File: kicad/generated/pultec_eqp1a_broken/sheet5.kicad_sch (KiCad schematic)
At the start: 20 parts, among them T3 core

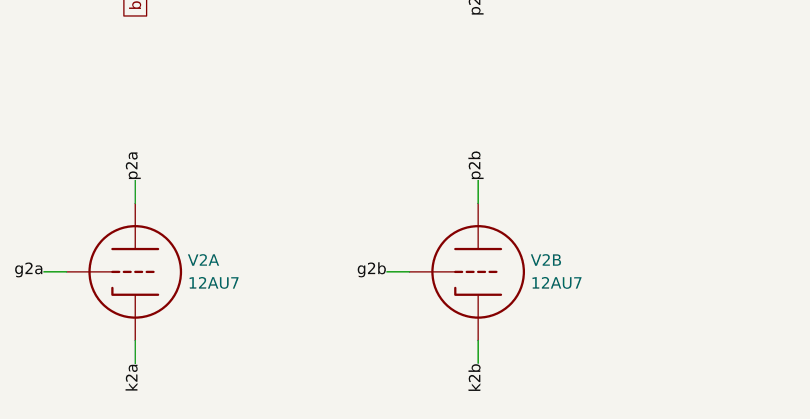
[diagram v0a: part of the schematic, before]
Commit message: Component editor C1: device files are pinned component versions
Device files move to config/components/<name>/<N>.yaml (the twelve former
config/devices/*.yaml are version 1, bytes unchanged), each version's sha256
(LF-normalized) in config/components/versions.lock. varimu/devices/versions.py
and varimu-circuit's versions.rs read the store the same way: a version edited
after saving is a load error, a bare name is the latest version for tools and
tests, and both builders refuse a bare name in a circuit. Circuits pin NAME@N:
the hand-written circuits, their device-choice parameters, the drawn circuits,
the symbol table's and both editors' placement defaults, the KiCad fixtures.
varimu fit-devices saves a new version only when a fit changed. The native
editor's model picker lists every version.

Every circuit builds identical IR and SPICE (export_circuit_fixtures --golden,
export_app_fixtures without a diff); the editor fixtures change only by the
pins. Tests: tests/test_versions.py, crates/varimu-circuit/tests/versions.rs,
editor_draw.rs (swapping a pinned version rebuilds; undo).

Co-Authored-By: Claude Opus 5.5 (1M context) <noreply@anthropic.com>
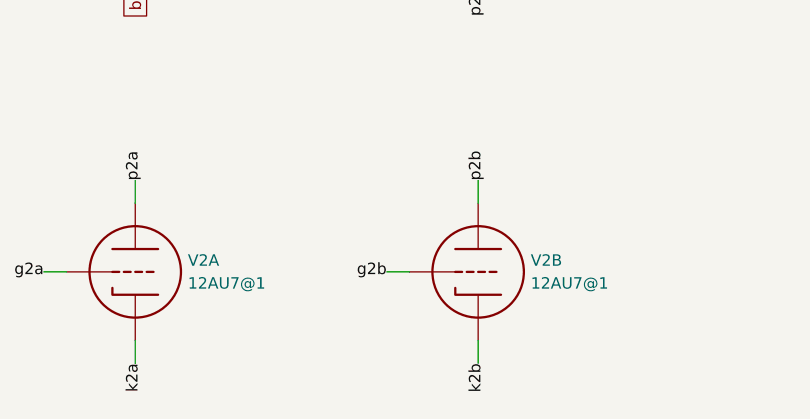
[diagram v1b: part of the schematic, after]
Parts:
- V2: value 12AU7 -> 12AU7@1
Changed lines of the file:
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@@
 			)
 		)
-		(property "Value" "12AU7"
+		(property "Value" "12AU7@1"
 			(at 82.042 115.57 0)
 			(effects
@@
 			)
 		)
-		(property "Value" "12AU7"
+		(property "Value" "12AU7@1"
 			(at 120.142 115.57 0)
 			(effects
